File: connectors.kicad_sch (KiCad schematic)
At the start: 2 parts, among them J1 Conn_01x04_Pin, J2 Conn_01x04_Pin

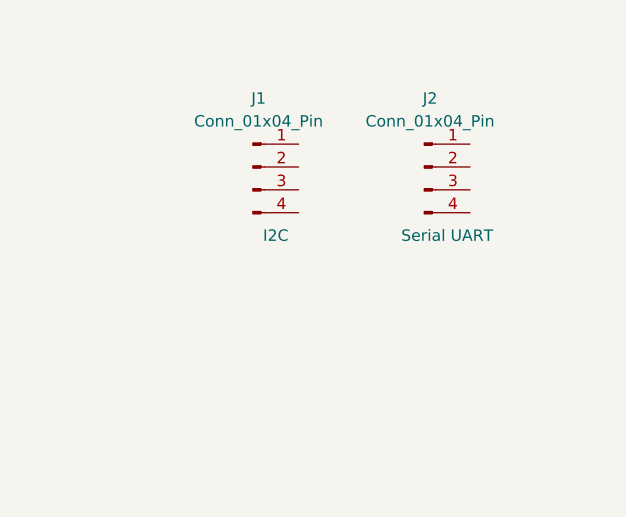
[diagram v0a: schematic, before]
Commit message: Added component values
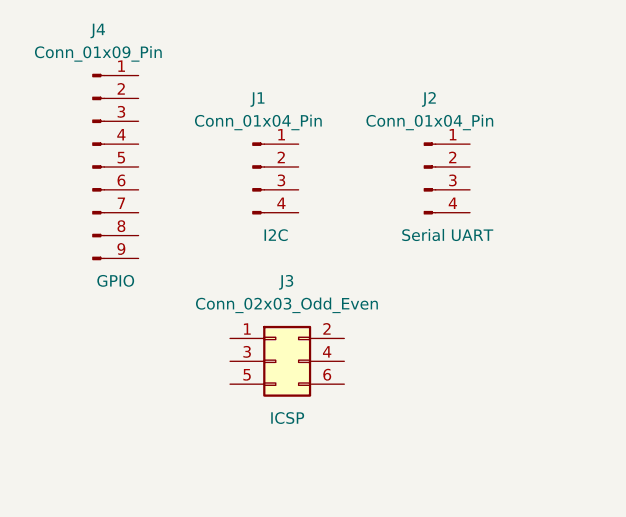
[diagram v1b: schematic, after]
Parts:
- added J3: Conn_02x03_Odd_Even, symbol Connector_Generic:Conn_02x03_Odd_Even
- added J4: Conn_01x09_Pin, symbol Connector:Conn_01x09_Pin
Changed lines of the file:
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@@
+    )
+  )
+  (symbol (lib_id "Connector_Generic:Conn_02x03_Odd_Even") (at 53.34 72.39 0) (unit 1)
+    (in_bom yes) (on_board yes) (dnp no)
+    (property "Reference" "J3" (at 54.61 63.5 0)
+      (effects (font (size 1.27 1.27)))
+    )
+    (property "Value" "Conn_02x03_Odd_Even" (at 54.61 66.04 0)
+      (effects (font (size 1.27 1.27)))
+    )
+    (property "Footprint" "" (at 53.34 72.39 0)
+      (effects (font (size 1.27 1.27)) hide)
+    )
+    (property "Datasheet" "~" (at 53.34 72.39 0)
+      (effects (font (size 1.27 1.27)) hide)
+    )
+    (property "Purpose" "ICSP" (at 54.61 78.74 0)
+      (effects (font (size 1.27 1.27)))
+    )
+    (pin "4")
+    (pin "3")
+    (pin "2")
+    (pin "6")
+    (pin "1")
+    (pin "5")
+    (instances
+      (project "mcu_datalogger"
+        (path "/2eb1960c-e24d-49a2-b353-c94e813acc08/a14294b5-ea75-478a-9800-c2102ded2188"
+          (reference "J3") (unit 1)
+        )
+      )
     )
   )
@@
         )
       )
+    )
+  )
+  (symbol (lib_id "Connector:Conn_01x09_Pin") (at 33.02 50.8 0) (unit 1)
+    (in_bom yes) (on_board yes) (dnp no)
+    (property "Reference" "J4" (at 33.655 35.56 0)
+      (effects (font (size 1.27 1.27)))
+    )
+    (property "Value" "Conn_01x09_Pin" (at 33.655 38.1 0)
+      (effects (font (size 1.27 1.27)))
+    )
+    (property "Footprint" "" (at 33.02 50.8 0)
+      (effects (font (size 1.27 1.27)) hide)
+    )
+    (property "Datasheet" "~" (at 33.02 50.8 0)
+      (effects (font (size 1.27 1.27)) hide)
+    )
+    (property "Purpose" "GPIO" (at 35.56 63.5 0)
+      (effects (font (size 1.27 1.27)))
+    )
+    (pin "6")
+    (pin "2")
+    (pin "5")
+    (pin "8")
+    (pin "7")
+    (pin "4")
+    (pin "1")
+    (pin "3")
+    (pin "9")
+    (instances
+      (project "mcu_datalogger"
+        (path "/2eb1960c-e24d-49a2-b353-c94e813acc08/a14294b5-ea75-478a-9800-c2102ded2188"
+          (reference "J4") (unit 1)
+        )
+      )

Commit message: Footprints assigned
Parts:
- J1, J2: footprint (none) -> Connector_PinHeader_2.54mm:PinHeader_1x04_P2.54mm_Vertical
- J3: footprint (none) -> Connector_PinHeader_2.54mm:PinHeader_2x03_P2.54mm_Vertical
- J4: footprint (none) -> Connector_PinHeader_2.54mm:PinHeader_1x09_P2.54mm_Vertical
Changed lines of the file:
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@@
       (effects (font (size 1.27 1.27)))
     )
-    (property "Footprint" "" (at 69.85 50.8 0)
+    (property "Footprint" "Connector_PinHeader_2.54mm:PinHeader_1x04_P2.54mm_Vertical" (at 69.85 50.8 0)
       (effects (font (size 1.27 1.27)) hide)
     )
@@
       (effects (font (size 1.27 1.27)))
     )
-    (property "Footprint" "" (at 53.34 72.39 0)
+    (property "Footprint" "Connector_PinHeader_2.54mm:PinHeader_2x03_P2.54mm_Vertical" (at 53.34 72.39 0)
       (effects (font (size 1.27 1.27)) hide)
     )
@@
       (effects (font (size 1.27 1.27)))
     )
-    (property "Footprint" "" (at 50.8 50.8 0)
+    (property "Footprint" "Connector_PinHeader_2.54mm:PinHeader_1x04_P2.54mm_Vertical" (at 50.8 50.8 0)
       (effects (font (size 1.27 1.27)) hide)
     )
@@
       (effects (font (size 1.27 1.27)))
     )
-    (property "Footprint" "" (at 33.02 50.8 0)
+    (property "Footprint" "Connector_PinHeader_2.54mm:PinHeader_1x09_P2.54mm_Vertical" (at 33.02 50.8 0)
       (effects (font (size 1.27 1.27)) hide)
     )

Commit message: Wiring done
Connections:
- net GND: now reaches J2.1 (Pin_1)
- net GND: now also J1.1 (Pin_1), J3.6 (Pin_6), J4.8 (Pin_8)
- net VCC: now reaches J2.2 (Pin_2)
- net VCC: now also J1.2 (Pin_2), J3.2 (Pin_2), J4.9 (Pin_9)
- net RX: now reaches J2.3 (Pin_3)
- net TX: now reaches J2.4 (Pin_4)
- net MISO: now reaches J3.1 (Pin_1)
- net SCK: now reaches J3.3 (Pin_3)
- net SCK: now also J1.4 (Pin_4)
- net MOSI: now reaches J3.4 (Pin_4)
- net RESET: now reaches J3.5 (Pin_5)
- net SDA: now reaches J1.3 (Pin_3)
- net D2: now reaches J4.1 (Pin_1)
- net D3: now reaches J4.2 (Pin_2)
- net D4: now reaches J4.3 (Pin_3)
- net D5: now reaches J4.4 (Pin_4)
- net D6: now reaches J4.5 (Pin_5)
- net D7: now reaches J4.6 (Pin_6)
- net D8: now reaches J4.7 (Pin_7)
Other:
- moved on the sheet: J1, J2, J3, J4
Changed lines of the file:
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@@
 (kicad_sch (version 20230121) (generator eeschema)
   (paper "A4")
-  (symbol (lib_id "Connector:Conn_01x04_Pin") (at 69.85 50.8 0) (unit 1)
+  (hierarchical_label "GND" (shape passive) (at 52.07 44.45 0) (fields_autoplaced)
+    (effects (font (size 1.27 1.27)) (justify left))
+  )
+  (hierarchical_label "SCK" (shape passive) (at 52.07 52.07 0) (fields_autoplaced)
+    (effects (font (size 1.27 1.27)) (justify left))
+  )
+  (hierarchical_label "MISO" (shape output) (at 69.85 72.39 180) (fields_autoplaced)
+    (effects (font (size 1.27 1.27)) (justify right))
+  )
+  (hierarchical_label "D3" (shape bidirectional) (at 49.53 66.04 0) (fields_autoplaced)
+    (effects (font (size 1.27 1.27)) (justify left))
+  )
+  (hierarchical_label "D7" (shape bidirectional) (at 49.53 76.2 0) (fields_autoplaced)
+    (effects (font (size 1.27 1.27)) (justify left))
+  )
+  (hierarchical_label "MOSI" (shape input) (at 82.55 74.93 0) (fields_autoplaced)
+    (effects (font (size 1.27 1.27)) (justify left))
+  )
+  (hierarchical_label "TX" (shape output) (at 78.74 50.8 0) (fields_autoplaced)
+    (effects (font (size 1.27 1.27)) (justify left))
+  )
+  (hierarchical_label "GND" (shape passive) (at 82.55 77.47 0) (fields_autoplaced)
+    (effects (font (size 1.27 1.27)) (justify left))
+  )
+  (hierarchical_label "SDA" (shape bidirectional) (at 52.07 49.53 0) (fields_autoplaced)
+    (effects (font (size 1.27 1.27)) (justify left))
+  )
+  (hierarchical_label "D4" (shape bidirectional) (at 49.53 68.58 0) (fields_autoplaced)
+    (effects (font (size 1.27 1.27)) (justify left))
+  )
+  (hierarchical_label "GND" (shape passive) (at 78.74 43.18 0) (fields_autoplaced)
+    (effects (font (size 1.27 1.27)) (justify left))
+  )
+  (hierarchical_label "VCC" (shape passive) (at 52.07 46.99 0) (fields_autoplaced)
+    (effects (font (size 1.27 1.27)) (justify left))
+  )
+  (hierarchical_label "D5" (shape bidirectional) (at 49.53 71.12 0) (fields_autoplaced)
+    (effects (font (size 1.27 1.27)) (justify left))
+  )
+  (hierarchical_label "D8" (shape bidirectional) (at 49.53 78.74 0) (fields_autoplaced)
+    (effects (font (size 1.27 1.27)) (justify left))
+  )
+  (hierarchical_label "VCC" (shape passive) (at 78.74 45.72 0) (fields_autoplaced)
+    (effects (font (size 1.27 1.27)) (justify left))
+  )
+  (hierarchical_label "GND" (shape passive) (at 49.53 81.28 0) (fields_autoplaced)
+    (effects (font (size 1.27 1.27)) (justify left))
+  )
+  (hierarchical_label "VCC" (shape passive) (at 49.53 83.82 0) (fields_autoplaced)
+    (effects (font (size 1.27 1.27)) (justify left))
+  )
+  (hierarchical_label "SCK" (shape passive) (at 69.85 74.93 180) (fields_autoplaced)
+    (effects (font (size 1.27 1.27)) (justify right))
+  )
+  (hierarchical_label "VCC" (shape passive) (at 82.55 72.39 0) (fields_autoplaced)
+    (effects (font (size 1.27 1.27)) (justify left))
+  )
+  (hierarchical_label "RX" (shape input) (at 78.74 48.26 0) (fields_autoplaced)
+    (effects (font (size 1.27 1.27)) (justify left))
+  )
+  (hierarchical_label "RESET" (shape passive) (at 69.85 77.47 180) (fields_autoplaced)
+    (effects (font (size 1.27 1.27)) (justify right))
+  )
+  (hierarchical_label "D2" (shape bidirectional) (at 49.53 63.5 0) (fields_autoplaced)
+    (effects (font (size 1.27 1.27)) (justify left))
+  )
+  (hierarchical_label "D6" (shape bidirectional) (at 49.53 73.66 0) (fields_autoplaced)
+    (effects (font (size 1.27 1.27)) (justify left))
+  )
+  (symbol (lib_id "Connector:Conn_01x04_Pin") (at 73.66 45.72 0) (unit 1)
     (in_bom yes) (on_board yes) (dnp no)
-    (property "Reference" "J2" (at 70.485 43.18 0)
+    (property "Reference" "J2" (at 74.295 38.1 0)
       (effects (font (size 1.27 1.27)))
     )
-    (property "Value" "Conn_01x04_Pin" (at 70.485 45.72 0)
+    (property "Value" "Conn_01x04_Pin" (at 74.295 40.64 0)
       (effects (font (size 1.27 1.27)))
     )
-    (property "Footprint" "Connector_PinHeader_2.54mm:PinHeader_1x04_P2.54mm_Vertical" (at 69.85 50.8 0)
+    (property "Footprint" "Connector_PinHeader_2.54mm:PinHeader_1x04_P2.54mm_Vertical" (at 73.66 45.72 0)
       (effects (font (size 1.27 1.27)) hide)
     )
-    (property "Datasheet" "~" (at 69.85 50.8 0)
+    (property "Datasheet" "~" (at 73.66 45.72 0)
       (effects (font (size 1.27 1.27)) hide)
     )
-    (property "Purpose" "Serial UART" (at 72.39 58.42 0)
+    (property "Purpose" "Serial UART" (at 76.2 53.34 0)
       (effects (font (size 1.27 1.27)))
     )
@@
     )
   )
-  (symbol (lib_id "Connector_Generic:Conn_02x03_Odd_Even") (at 53.34 72.39 0) (unit 1)
+  (symbol (lib_id "Connector_Generic:Conn_02x03_Odd_Even") (at 74.93 74.93 0) (unit 1)
     (in_bom yes) (on_board yes) (dnp no)
-    (property "Reference" "J3" (at 54.61 63.5 0)
+    (property "Reference" "J3" (at 76.2 66.04 0)
       (effects (font (size 1.27 1.27)))
     )
-    (property "Value" "Conn_02x03_Odd_Even" (at 54.61 66.04 0)
+    (property "Value" "Conn_02x03_Odd_Even" (at 76.2 68.58 0)
       (effects (font (size 1.27 1.27)))
     )
-    (property "Footprint" "Connector_PinHeader_2.54mm:PinHeader_2x03_P2.54mm_Vertical" (at 53.34 72.39 0)
+    (property "Footprint" "Connector_PinHeader_2.54mm:PinHeader_2x03_P2.54mm_Vertical" (at 74.93 74.93 0)
       (effects (font (size 1.27 1.27)) hide)
     )
-    (property "Datasheet" "~" (at 53.34 72.39 0)
+    (property "Datasheet" "~" (at 74.93 74.93 0)
       (effects (font (size 1.27 1.27)) hide)
     )
-    (property "Purpose" "ICSP" (at 54.61 78.74 0)
+    (property "Purpose" "ICSP" (at 76.2 81.28 0)
       (effects (font (size 1.27 1.27)))
     )
@@
     )
   )
-  (symbol (lib_id "Connector:Conn_01x04_Pin") (at 50.8 50.8 0) (unit 1)
+  (symbol (lib_id "Connector:Conn_01x04_Pin") (at 46.99 46.99 0) (unit 1)
     (in_bom yes) (on_board yes) (dnp no)
-    (property "Reference" "J1" (at 51.435 43.18 0)
+    (property "Reference" "J1" (at 47.625 39.37 0)
       (effects (font (size 1.27 1.27)))
     )
-    (property "Value" "Conn_01x04_Pin" (at 51.435 45.72 0)
+    (property "Value" "Conn_01x04_Pin" (at 47.625 41.91 0)
       (effects (font (size 1.27 1.27)))
     )
-    (property "Footprint" "Connector_PinHeader_2.54mm:PinHeader_1x04_P2.54mm_Vertical" (at 50.8 50.8 0)
+    (property "Footprint" "Connector_PinHeader_2.54mm:PinHeader_1x04_P2.54mm_Vertical" (at 46.99 46.99 0)
       (effects (font (size 1.27 1.27)) hide)
     )
-    (property "Datasheet" "~" (at 50.8 50.8 0)
+    (property "Datasheet" "~" (at 46.99 46.99 0)
       (effects (font (size 1.27 1.27)) hide)
     )
-    (property "Purpose" "I2C" (at 53.34 58.42 0)
+    (property "Purpose" "I2C" (at 49.53 54.61 0)
       (effects (font (size 1.27 1.27)))
     )
@@
     )
   )
-  (symbol (lib_id "Connector:Conn_01x09_Pin") (at 33.02 50.8 0) (unit 1)
+  (symbol (lib_id "Connector:Conn_01x09_Pin") (at 44.45 73.66 0) (unit 1)
     (in_bom yes) (on_board yes) (dnp no)
-    (property "Reference" "J4" (at 33.655 35.56 0)
+    (property "Reference" "J4" (at 45.085 58.42 0)
       (effects (font (size 1.27 1.27)))
     )
-    (property "Value" "Conn_01x09_Pin" (at 33.655 38.1 0)
+    (property "Value" "Conn_01x09_Pin" (at 45.085 60.96 0)
       (effects (font (size 1.27 1.27)))
     )
-    (property "Footprint" "Connector_PinHeader_2.54mm:PinHeader_1x09_P2.54mm_Vertical" (at 33.02 50.8 0)
+    (property "Footprint" "Connector_PinHeader_2.54mm:PinHeader_1x09_P2.54mm_Vertical" (at 44.45 73.66 0)
       (effects (font (size 1.27 1.27)) hide)
     )
-    (property "Datasheet" "~" (at 33.02 50.8 0)
+    (property "Datasheet" "~" (at 44.45 73.66 0)
       (effects (font (size 1.27 1.27)) hide)
     )
-    (property "Purpose" "GPIO" (at 35.56 63.5 0)
+    (property "Purpose" "GPIO" (at 46.99 86.36 0)
       (effects (font (size 1.27 1.27)))
     )
